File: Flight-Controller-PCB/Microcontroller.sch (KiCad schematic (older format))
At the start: 37 parts, among them J9 USB_B_Micro, Q3 Q_PMOS_GSD, Q4 Q_PMOS_GSD, SW1 Push-Switch, U3 ATmega32U4-AU, U4 NCP1117-5.0, U5 LP2985-3.3, Y1 16MHz, CL 7pF

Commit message: Microcontroller reviewed
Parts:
- removed U4: NCP1117-5.0, Package_TO_SOT_SMD:SOT-223-3_TabPin2, symbol Regulator_Linear:NCP1117-5.0_SOT223
- added C17: 10uF 20V 20%, Capacitor_SMD:C_0603_1608Metric_Pad1.05x0.95mm_HandSolder, symbol Device:CP
- added C18: 1uF 12V X7R 10%, Capacitor_SMD:C_0603_1608Metric_Pad1.05x0.95mm_HandSolder, symbol Device:C
- added U4: LM1117-5.0, Package_TO_SOT_SMD:SOT-223, symbol Custom:LM1117-5.0
- D4: value D -> 75V 150mA; footprint (none) -> Diode_SMD:D_0603_1608Metric_Pad1.05x0.95mm_HandSolder; Digi-Key # (none) -> TS4148CRZGCT-ND; Digi-Key LinkDigi LinkDigi-Key Link (none) -> https://www.digikey.ca/en/products/detail/taiwan-semiconduc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; Manufacturer (none) -> Taiwan Semiconductor Corporation; Manufacturer # (none) -> TS4148C RZG
- FB1: footprint (none) -> Diode_SMD:D_0603_1608Metric_Pad1.05x0.95mm_HandSolder; Digi-Key # (none) -> MH1608-300YCT-ND; Digi-Key LinkDigi LinkDigi-Key Link (none) -> https://www.digikey.ca/en/products/detail/bourns-inc/MH1608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; Manufacturer (none) -> Bourns Inc.; Manufacturer # (none) -> MH1608-300Y
- SW1: Digi-Key # (none) -> CKN10361CT-ND; Digi-Key LinkDigi LinkDigi-Key Link (none) -> https://www.digikey.ca/en/products/detail/c-k/RS-187R05A2-D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; Manufacturer (none) -> C&K; Manufacturer # (none) -> RS-187R05A2-DS MT RT
- U5: Digi-Key # (none) -> 296-18476-1-ND; Digi-Key LinkDigi LinkDigi-Key Link (none) -> https://www.digikey.ca/en/products/detail/texas-instruments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; Manufacturer (none) -> Texas Instruments; Manufacturer # (none) -> LP2985-33DBVR
- renumbered C17 to C19, C19 to C20, C20 to C21, C18 to C22
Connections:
- net +5V: now also C12.1, FB1.1, U3.24 (AVCC), U3.44 (AVCC), C18.1, U4.2 (VO), U4.4
- net GND: now also C17.2, C18.2, U4.1 (GND)
- net at C16.1, Q4.2 (S): now also C17.1, U4.3 (VI)
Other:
- moved on the sheet: C16, C22, U5

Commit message: clean up refernces
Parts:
- C11, C12, C18, C22: value 1uF 12V X7R 10% -> 1uF 16V X7R 10%
- C20: value 22uF 10V 20% -> 22uF 16V 20%
- D5, D6: value LED -> Orange 2V 20mA
- FB1: value Ferrite_Bead -> Ferrite 30 ohm 1 line
- Q3, Q4: value Q_PMOS_GSD -> PMV48XP,215
- R15, R16: value 1 kohm -> 1 kohm 5%
- R17: value 10 kohm -> 10 kohm 5%
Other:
- moved on the sheet: D5, D6
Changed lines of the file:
@@
 P 6400 3300
 F 0 "Q3" V 6651 3300 50  0000 C CNN
-F 1 "Q_PMOS_GSD" V 6742 3300 50  0000 C CNN
+F 1 "PMV48XP,215" V 6742 3300 50  0000 C CNN
 F 2 "Package_TO_SOT_SMD:SOT-23" H 6600 3400 50  0001 C CNN
 F 3 "~" H 6400 3300 50  0001 C CNN
@@
 P 6600 1600
 F 0 "Q4" V 6851 1600 50  0000 C CNN
-F 1 "Q_PMOS_GSD" V 6942 1600 50  0000 C CNN
+F 1 "PMV48XP,215" V 6942 1600 50  0000 C CNN
 F 2 "Package_TO_SOT_SMD:SOT-23" H 6800 1700 50  0001 C CNN
 F 3 "~" H 6600 1600 50  0001 C CNN
@@
 AR Path="/5FDD4B9C/6016A3D7" Ref="C22"  Part="1"
 F 0 "C22" H 9515 3446 50  0000 L CNN
-F 1 "1uF 12V X7R 10%" H 9515 3355 50  0000 L CNN
+F 1 "1uF 16V X7R 10%" H 9515 3355 50  0000 L CNN
 F 2 "Capacitor_SMD:C_0603_1608Metric_Pad1.05x0.95mm_HandSolder" H 9438 3250 50  0001 C CNN
 F 3 "~" H 9400 3400 50  0001 C CNN
@@
 P 9250 5650
 F 0 "C20" H 9132 5696 50  0000 R CNN
-F 1 "22uF 10V 20%" H 9132 5605 50  0000 R CNN
+F 1 "22uF 16V 20%" H 9132 5605 50  0000 R CNN
 F 2 "Capacitor_SMD:C_0603_1608Metric_Pad1.05x0.95mm_HandSolder" H 9288 5500 50  0001 C CNN
 F 3 "~" H 9250 5650 50  0001 C CNN
@@
 P 3050 1600
 F 0 "FB1" H 2913 1554 50  0000 R CNN
-F 1 "Ferrite_Bead" H 2913 1645 50  0000 R CNN
+F 1 "Ferrite 30 ohm 1 line" H 2913 1645 50  0000 R CNN
 F 2 "Diode_SMD:D_0603_1608Metric_Pad1.05x0.95mm_HandSolder" V 2980 1600 50  0001 C CNN
 F 3 "~" H 3050 1600 50  0001 C CNN
@@
 AR Path="/5FDD4B9C/6013640D" Ref="R17"  Part="1"
 F 0 "R17" V 4507 4450 50  0000 C CNN
-F 1 "10 kohm" V 4416 4450 50  0000 C CNN
+F 1 "10 kohm 5%" V 4416 4450 50  0000 C CNN
 F 2 "Resistor_SMD:R_0603_1608Metric_Pad1.05x0.95mm_HandSolder" V 4230 4450 50  0001 C CNN
 F 3 "~" H 4300 4450 50  0001 C CNN
@@
 AR Path="/5FDD4B9C/602BA879" Ref="C11"  Part="1"
 F 0 "C11" H 2365 1946 50  0000 L CNN
-F 1 "1uF 12V X7R 10%" H 2365 1855 50  0000 L CNN
+F 1 "1uF 16V X7R 10%" H 2365 1855 50  0000 L CNN
 F 2 "Capacitor_SMD:C_0603_1608Metric_Pad1.05x0.95mm_HandSolder" H 2288 1750 50  0001 C CNN
 F 3 "~" H 2250 1900 50  0001 C CNN
@@
 AR Path="/5FDD4B9C/603D5C78" Ref="R16"  Part="1"
 F 0 "R16" V 4507 4050 50  0000 C CNN
-F 1 "1 kohm" V 4416 4050 50  0000 C CNN
+F 1 "1 kohm 5%" V 4416 4050 50  0000 C CNN
 F 2 "Resistor_SMD:R_0603_1608Metric_Pad1.05x0.95mm_HandSolder" V 4230 4050 50  0001 C CNN
 F 3 "~" H 4300 4050 50  0001 C CNN
@@
 AR Path="/5FDD4B9C/603DB557" Ref="R15"  Part="1"
 F 0 "R15" V 4507 2350 50  0000 C CNN
-F 1 "1 kohm" V 4416 2350 50  0000 C CNN
+F 1 "1 kohm 5%" V 4416 2350 50  0000 C CNN
 F 2 "Resistor_SMD:R_0603_1608Metric_Pad1.05x0.95mm_HandSolder" V 4230 2350 50  0001 C CNN
 F 3 "~" H 4300 2350 50  0001 C CNN
@@
 L Device:LED D?
 U 1 1 603F28D0
-P 4700 2350
+P 4900 2350
 AR Path="/603F28D0" Ref="D?"  Part="1"
 AR Path="/5FDD4B9C/603F28D0" Ref="D5"  Part="1"
-F 0 "D5" H 4693 2095 50  0000 C CNN
-F 1 "LED" H 4693 2186 50  0000 C CNN
-F 2 "LED_SMD:LED_0603_1608Metric_Pad1.05x0.95mm_HandSolder" H 4700 2350 50  0001 C CNN
-F 3 "~" H 4700 2350 50  0001 C CNN
-	1    4700 2350
+F 0 "D5" H 4893 2095 50  0000 C CNN
+F 1 "Orange 2V 20mA" H 4893 2186 50  0000 C CNN
+F 2 "LED_SMD:LED_0603_1608Metric_Pad1.05x0.95mm_HandSolder" H 4900 2350 50  0001 C CNN
+F 3 "~" H 4900 2350 50  0001 C CNN
+	1    4900 2350
 	-1   0    0    1
 $EndComp
@@
 L Device:LED D?
 U 1 1 603F8424
-P 4700 4050
+P 4900 4050
 AR Path="/603F8424" Ref="D?"  Part="1"
 AR Path="/5FDD4B9C/603F8424" Ref="D6"  Part="1"
-F 0 "D6" H 4693 3795 50  0000 C CNN
-F 1 "LED" H 4693 3886 50  0000 C CNN
-F 2 "LED_SMD:LED_0603_1608Metric_Pad1.05x0.95mm_HandSolder" H 4700 4050 50  0001 C CNN
-F 3 "~" H 4700 4050 50  0001 C CNN
-	1    4700 4050
+F 0 "D6" H 4893 3795 50  0000 C CNN
+F 1 "Orange 2V 20mA" H 4893 3886 50  0000 C CNN
+F 2 "LED_SMD:LED_0603_1608Metric_Pad1.05x0.95mm_HandSolder" H 4900 4050 50  0001 C CNN
+F 3 "~" H 4900 4050 50  0001 C CNN
+	1    4900 4050
 	-1   0    0    1
 $EndComp
@@
 L power:GND #PWR062
 U 1 1 603FDF8A
-P 4950 4050
-F 0 "#PWR062" H 4950 3800 50  0001 C CNN
-F 1 "GND" H 4955 3877 50  0000 C CNN
-F 2 "" H 4950 4050 50  0001 C CNN
-F 3 "" H 4950 4050 50  0001 C CNN
-	1    4950 4050
+P 5150 4050
+F 0 "#PWR062" H 5150 3800 50  0001 C CNN
+F 1 "GND" H 5155 3877 50  0000 C CNN
+F 2 "" H 5150 4050 50  0001 C CNN
+F 3 "" H 5150 4050 50  0001 C CNN
+	1    5150 4050
 	1    0    0    -1
 $EndComp
@@
 L power:GND #PWR061
 U 1 1 604038A5
-P 4950 2350
-F 0 "#PWR061" H 4950 2100 50  0001 C CNN
-F 1 "GND" H 4955 2177 50  0000 C CNN
-F 2 "" H 4950 2350 50  0001 C CNN
-F 3 "" H 4950 2350 50  0001 C CNN
-	1    4950 2350
-	1    0    0    -1
-$EndComp
-Wire Wire Line
-	4450 2350 4550 2350
-Wire Wire Line
-	4850 2350 4950 2350
-Wire Wire Line
-	4450 4050 4550 4050
-Wire Wire Line
-	4850 4050 4950 4050
+P 5150 2350
+F 0 "#PWR061" H 5150 2100 50  0001 C CNN
+F 1 "GND" H 5155 2177 50  0000 C CNN
+F 2 "" H 5150 2350 50  0001 C CNN
+F 3 "" H 5150 2350 50  0001 C CNN
+	1    5150 2350
+	1    0    0    -1
+$EndComp
+Wire Wire Line
+	5050 2350 5150 2350
+Wire Wire Line
+	5050 4050 5150 4050
 Connection ~ 7900 5400
 Wire Wire Line
@@
 AR Path="/5FDD4B9C/607F5DBA" Ref="C18"  Part="1"
 F 0 "C18" H 8215 3446 50  0000 L CNN
-F 1 "1uF 12V X7R 10%" H 8215 3355 50  0000 L CNN
+F 1 "1uF 16V X7R 10%" H 8215 3355 50  0000 L CNN
 F 2 "Capacitor_SMD:C_0603_1608Metric_Pad1.05x0.95mm_HandSolder" H 8138 3250 50  0001 C CNN
 F 3 "~" H 8100 3400 50  0001 C CNN
@@
 AR Path="/5FDD4B9C/605F1BA8" Ref="C12"  Part="1"
 F 0 "C12" H 3765 1946 50  0000 L CNN
-F 1 "1uF 12V X7R 10%" H 3765 1855 50  0000 L CNN
+F 1 "1uF 16V X7R 10%" H 3765 1855 50  0000 L CNN
 F 2 "Capacitor_SMD:C_0603_1608Metric_Pad1.05x0.95mm_HandSolder" H 3688 1750 50  0001 C CNN
 F 3 "~" H 3650 1900 50  0001 C CNN
@@
 Wire Wire Line
 	3050 1900 3050 1750
+Wire Wire Line
+	4450 2350 4750 2350
+Wire Wire Line
+	4450 4050 4750 4050
 $EndSCHEMATC

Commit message: Create BOM and schematic
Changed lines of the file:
@@
 AR Path="/5FD9E07D/6008B98A" Ref="C?"  Part="1"
 AR Path="/5FDD4B9C/6008B98A" Ref="C16"  Part="1"
-F 0 "C16" V 7350 1850 50  0000 R CNN
+F 0 "C16" V 7350 1750 50  0000 R CNN
 F 1 "0.1uF 20V X7R 10%" V 7250 2050 50  0000 R CNN
 F 2 "Capacitor_SMD:C_0603_1608Metric_Pad1.05x0.95mm_HandSolder" H 7138 1650 50  0001 C CNN
@@
 AR Path="/5FD9E07D/600D6400" Ref="C?"  Part="1"
 AR Path="/5FDD4B9C/600D6400" Ref="C21"  Part="1"
-F 0 "C21" V 9650 1850 50  0000 R CNN
+F 0 "C21" V 9650 1750 50  0000 R CNN
 F 1 "0.1uF 16V X7R 10%" V 9550 2050 50  0000 R CNN
 F 2 "Capacitor_SMD:C_0603_1608Metric_Pad1.05x0.95mm_HandSolder" H 9438 1650 50  0001 C CNN

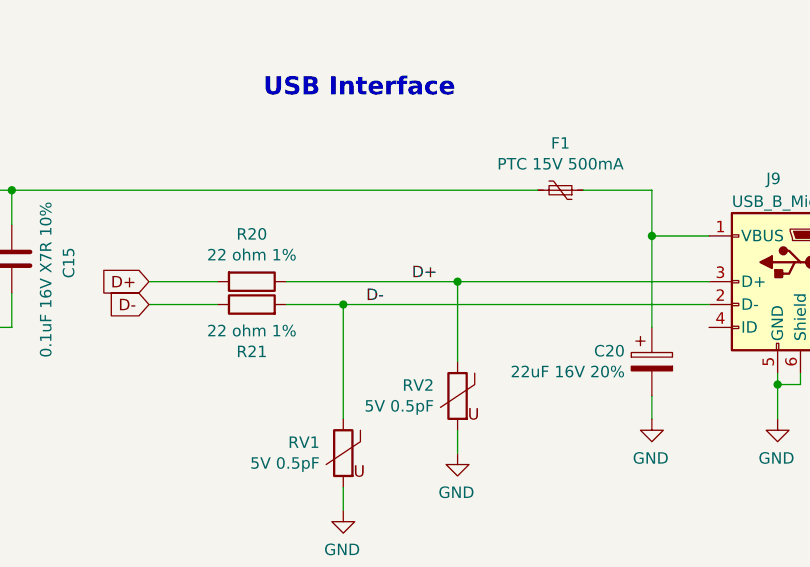
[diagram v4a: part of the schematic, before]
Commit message: Power regulators routed
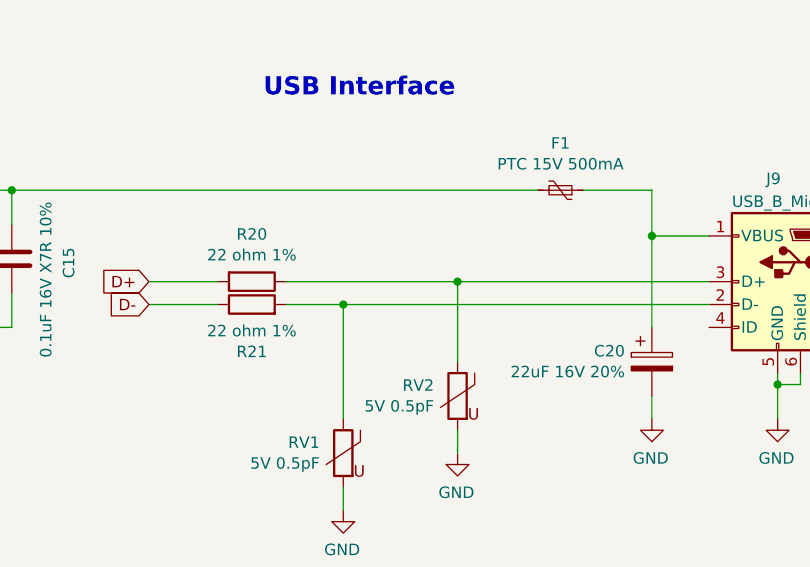
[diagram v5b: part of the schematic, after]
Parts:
- RV1, RV2: footprint Diode_SMD:D_0603_1608Metric_Pad1.05x0.95mm_HandSolder -> Resistor_SMD:R_0603_1608Metric_Pad1.05x0.95mm_HandSolder
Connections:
- net D+: no longer J9.3 (D+), R20.1, RV2.1
- net D-: no longer J9.2 (D-), R21.2, RV1.1
- new net: J9.2 (D-), R21.2, RV1.1
- new net: J9.3 (D+), R20.1, RV2.1
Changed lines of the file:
@@
 F 0 "RV1" H 8003 6096 50  0000 L CNN
 F 1 "5V 0.5pF" H 8003 6005 50  0000 L CNN
-F 2 "Diode_SMD:D_0603_1608Metric_Pad1.05x0.95mm_HandSolder" V 7830 6050 50  0001 C CNN
+F 2 "Resistor_SMD:R_0603_1608Metric_Pad1.05x0.95mm_HandSolder" V 7830 6050 50  0001 C CNN
 F 3 "~" H 7900 6050 50  0001 C CNN
 F 4 "Bourns Inc." H 7900 6050 50  0001 C CNN "Manufacturer"
@@
 F 0 "RV2" H 8503 5846 50  0000 L CNN
 F 1 "5V 0.5pF" H 8503 5755 50  0000 L CNN
-F 2 "Diode_SMD:D_0603_1608Metric_Pad1.05x0.95mm_HandSolder" V 8330 5800 50  0001 C CNN
+F 2 "Resistor_SMD:R_0603_1608Metric_Pad1.05x0.95mm_HandSolder" V 8330 5800 50  0001 C CNN
 F 3 "~" H 8400 5800 50  0001 C CNN
 F 4 "Bourns Inc." H 8400 5800 50  0001 C CNN "Manufacturer"
@@
 Wire Wire Line
 	8400 5950 8400 6050
-Text Label 8200 5300 0    50   ~ 0
-D+
-Text Label 8000 5400 0    50   ~ 0
-D-
 $Comp
 L Device:CP C20

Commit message: everything placed
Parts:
- added C?: 0.1uF 16V X7R 10%, Capacitor_SMD:C_0603_1608Metric_Pad1.05x0.95mm_HandSolder, symbol Device:C
- FB1: footprint Diode_SMD:D_0603_1608Metric_Pad1.05x0.95mm_HandSolder -> Resistor_SMD:R_0603_1608Metric_Pad1.05x0.95mm_HandSolder
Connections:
- net +5V: now also C?.1
- net GND: now also C?.2
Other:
- moved on the sheet: C11
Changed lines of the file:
@@
 AR Path="/5FDD4B9C/5FF2DBB2" Ref="C7"  Part="1"
 F 0 "C7" V 1352 2450 50  0000 C CNN
-F 1 "22pF 12V X7R 2%" V 1261 2450 50  0000 C CNN
+F 1 "22pF 12V X7R 2%" V 1250 2450 50  0000 C CNN
 F 2 "Capacitor_SMD:C_0603_1608Metric_Pad1.05x0.95mm_HandSolder" H 1138 2300 50  0001 C CNN
 F 3 "~" H 1100 2450 50  0001 C CNN
@@
 F 0 "FB1" H 2913 1554 50  0000 R CNN
 F 1 "Ferrite 30 ohm 1 line" H 2913 1645 50  0000 R CNN
-F 2 "Diode_SMD:D_0603_1608Metric_Pad1.05x0.95mm_HandSolder" V 2980 1600 50  0001 C CNN
+F 2 "Resistor_SMD:R_0603_1608Metric_Pad1.05x0.95mm_HandSolder" V 2980 1600 50  0001 C CNN
 F 3 "~" H 3050 1600 50  0001 C CNN
 F 4 "Bourns Inc." H 3050 1600 50  0001 C CNN "Manufacturer"
@@
 L Device:C C?
 U 1 1 602BA879
-P 2250 1900
+P 2350 1900
 AR Path="/5FD99B6C/602BA879" Ref="C?"  Part="1"
 AR Path="/5FD9E07D/602BA879" Ref="C?"  Part="1"
 AR Path="/5FDD4B9C/602BA879" Ref="C11"  Part="1"
-F 0 "C11" H 2365 1946 50  0000 L CNN
-F 1 "1uF 16V X7R 10%" H 2365 1855 50  0000 L CNN
-F 2 "Capacitor_SMD:C_0603_1608Metric_Pad1.05x0.95mm_HandSolder" H 2288 1750 50  0001 C CNN
-F 3 "~" H 2250 1900 50  0001 C CNN
-	1    2250 1900
+F 0 "C11" H 2465 1946 50  0000 L CNN
+F 1 "1uF 16V X7R 10%" H 2465 1855 50  0000 L CNN
+F 2 "Capacitor_SMD:C_0603_1608Metric_Pad1.05x0.95mm_HandSolder" H 2388 1750 50  0001 C CNN
+F 3 "~" H 2350 1900 50  0001 C CNN
+	1    2350 1900
 	-1   0    0    -1
 $EndComp
@@
 L power:GND #PWR052
 U 1 1 602BA87F
-P 2250 2050
-F 0 "#PWR052" H 2250 1800 50  0001 C CNN
-F 1 "GND" H 2255 1877 50  0000 C CNN
-F 2 "" H 2250 2050 50  0001 C CNN
-F 3 "" H 2250 2050 50  0001 C CNN
-	1    2250 2050
-	1    0    0    -1
-$EndComp
-Wire Wire Line
-	2250 1750 2850 1750
+P 2350 2050
+F 0 "#PWR052" H 2350 1800 50  0001 C CNN
+F 1 "GND" H 2355 1877 50  0000 C CNN
+F 2 "" H 2350 2050 50  0001 C CNN
+F 3 "" H 2350 2050 50  0001 C CNN
+	1    2350 2050
+	1    0    0    -1
+$EndComp
 Connection ~ 2850 1750
 Wire Wire Line
@@
 	1    0    0    -1
 $EndComp
+$Comp
+L Device:C C?
+U 1 1 600FEE9A
+P 1400 1900
+AR Path="/5FD99B6C/600FEE9A" Ref="C?"  Part="1"
+AR Path="/5FD9E07D/600FEE9A" Ref="C?"  Part="1"
+AR Path="/5FDD4B9C/600FEE9A" Ref="C?"  Part="1"
+F 0 "C?" H 1300 1900 50  0000 R CNN
+F 1 "0.1uF 16V X7R 10%" H 1350 2000 50  0000 R CNN
+F 2 "Capacitor_SMD:C_0603_1608Metric_Pad1.05x0.95mm_HandSolder" H 1438 1750 50  0001 C CNN
+F 3 "~" H 1400 1900 50  0001 C CNN
+	1    1400 1900
+	1    0    0    -1
+$EndComp
+$Comp
+L power:GND #PWR?
+U 1 1 6010BE74
+P 1400 2050
+F 0 "#PWR?" H 1400 1800 50  0001 C CNN
+F 1 "GND" H 1405 1877 50  0000 C CNN
+F 2 "" H 1400 2050 50  0001 C CNN
+F 3 "" H 1400 2050 50  0001 C CNN
+	1    1400 2050
+	1    0    0    -1
+$EndComp
+Connection ~ 2350 1750
+Wire Wire Line
+	2350 1750 2850 1750
+Wire Wire Line
+	1400 1750 2350 1750
 $EndSCHEMATC

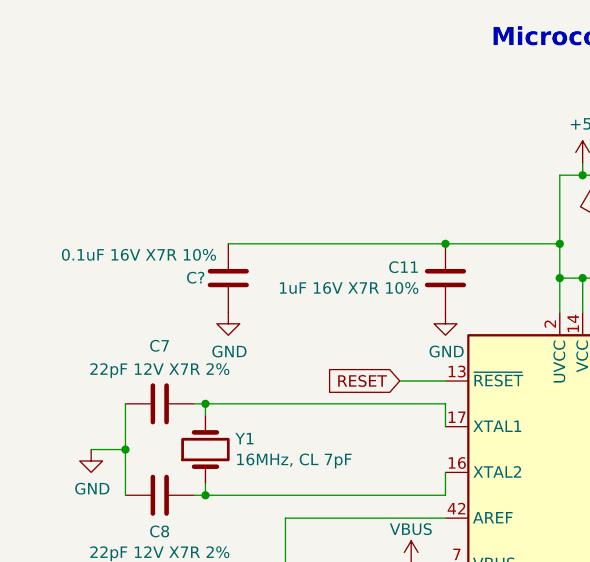
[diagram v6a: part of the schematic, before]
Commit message: Moved all components to the top of the board
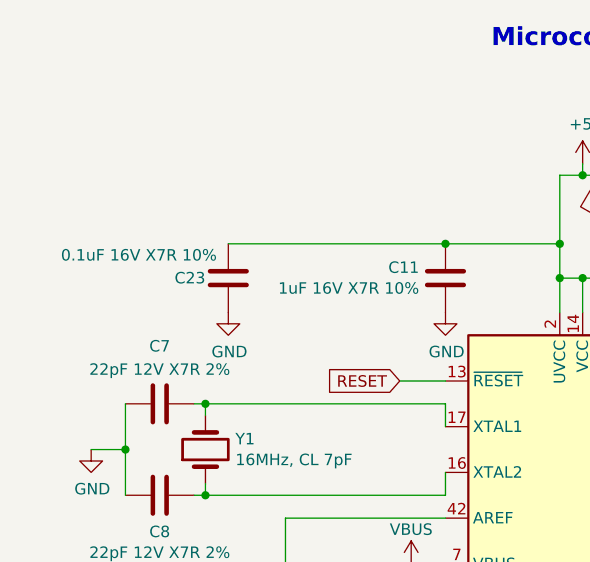
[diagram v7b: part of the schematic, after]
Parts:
- gave numbers to parts that had none: 1
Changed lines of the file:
@@
 AR Path="/5FD99B6C/600FEE9A" Ref="C?"  Part="1"
 AR Path="/5FD9E07D/600FEE9A" Ref="C?"  Part="1"
-AR Path="/5FDD4B9C/600FEE9A" Ref="C?"  Part="1"
-F 0 "C?" H 1300 1900 50  0000 R CNN
+AR Path="/5FDD4B9C/600FEE9A" Ref="C23"  Part="1"
+F 0 "C23" H 1300 1900 50  0000 R CNN
 F 1 "0.1uF 16V X7R 10%" H 1350 2000 50  0000 R CNN
 F 2 "Capacitor_SMD:C_0603_1608Metric_Pad1.05x0.95mm_HandSolder" H 1438 1750 50  0001 C CNN
@@
 $EndComp
 $Comp
-L power:GND #PWR?
+L power:GND #PWR0101
 U 1 1 6010BE74
 P 1400 2050
-F 0 "#PWR?" H 1400 1800 50  0001 C CNN
+F 0 "#PWR0101" H 1400 1800 50  0001 C CNN
 F 1 "GND" H 1405 1877 50  0000 C CNN
 F 2 "" H 1400 2050 50  0001 C CNN

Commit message: Resaved schematic
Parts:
- U3: symbol MCU_Microchip_ATmega:ATmega32U4-AU -> Flight-Controller-PCB-rescue:ATmega32U4-AU-MCU_Microchip_ATmega-Flight-Controller-PCB-rescue
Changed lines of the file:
@@
 EESchema Schematic File Version 4
-LIBS:Flight-Controller-PCB-cache
 EELAYER 30 0
 EELAYER END
@@
 	8900 2050 8900 1950
 $Comp
-L MCU_Microchip_ATmega:ATmega32U4-AU U3
+L Flight-Controller-PCB-rescue:ATmega32U4-AU-MCU_Microchip_ATmega-Flight-Controller-PCB-rescue U3
 U 1 1 5FE513CE
 P 2950 3850
+AR Path="/5FE513CE" Ref="U3"  Part="1"
+AR Path="/5FDD4B9C/5FE513CE" Ref="U3"  Part="1"
 F 0 "U3" H 2950 1961 50  0000 C CNN
 F 1 "ATmega32U4-AU" H 2950 1870 50  0000 C CNN
